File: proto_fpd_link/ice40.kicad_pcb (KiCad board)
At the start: 4 copper layers, 50 x 50 mm, 48 parts, among them J1 Conn_01x12, J101 Conn_02x05_Odd_Even, J102 Conn_01x18, J2 Conn_01x05, J3 Conn_01x19, J4 Conn_01x05, J5 Conn_01x01, J7 Conn_01x01, U101 TLV71333PDBV, U102 iCE40HX1K-CB132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

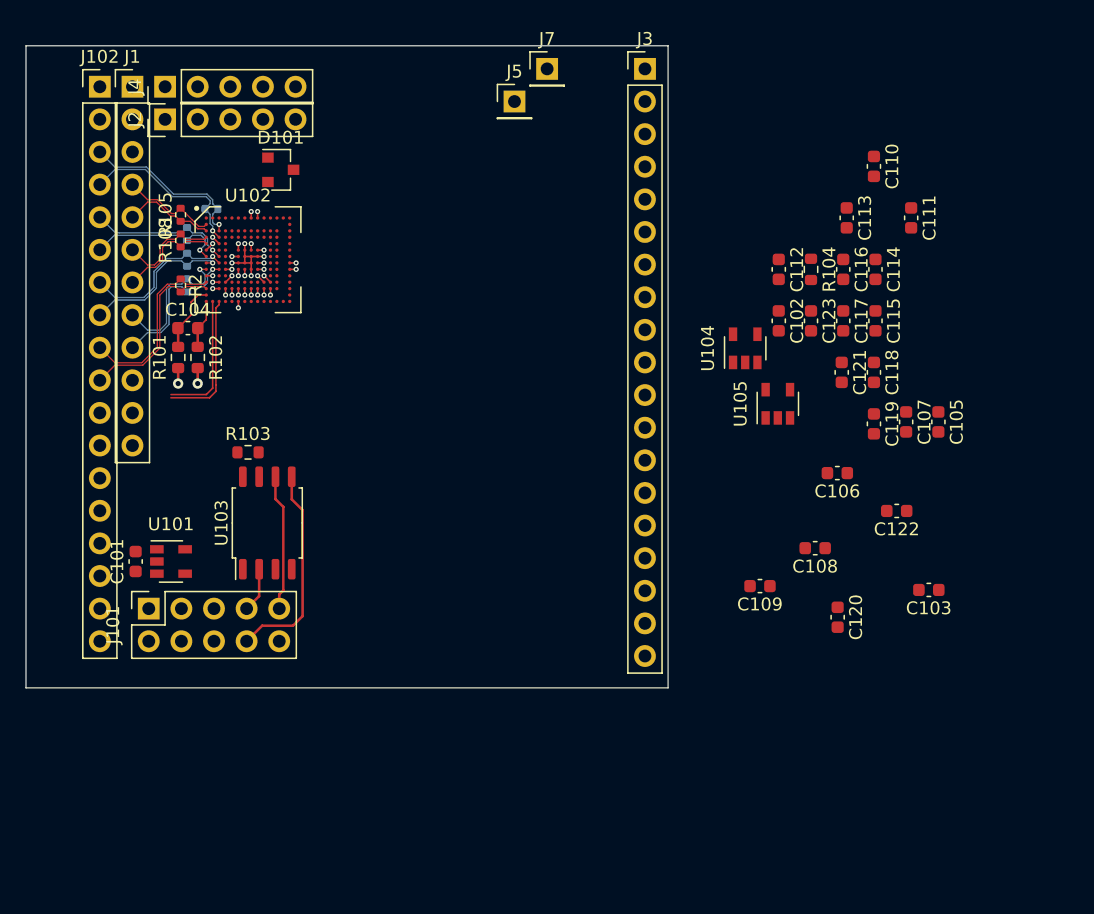
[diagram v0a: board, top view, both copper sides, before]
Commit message: initial commit of ice40 programmer board
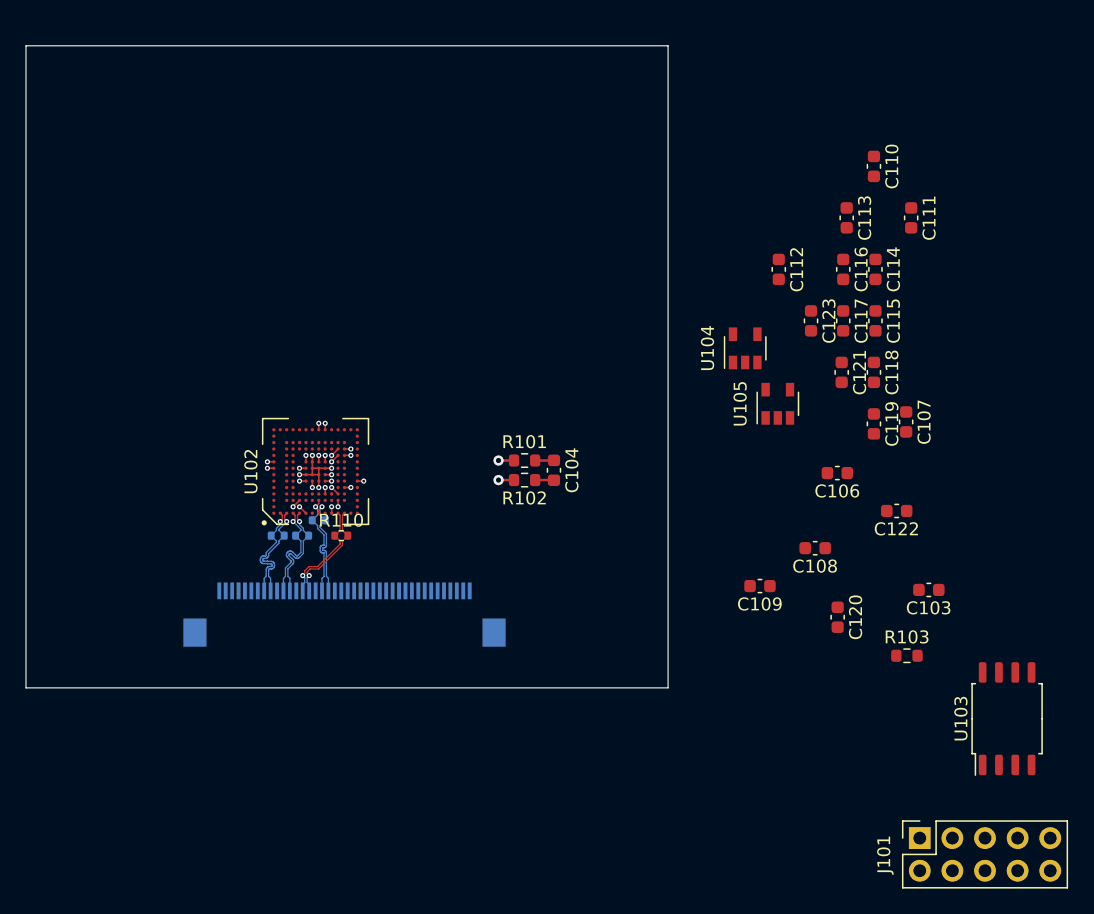
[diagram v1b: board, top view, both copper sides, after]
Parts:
- removed C101, C102, C105: 100n, Capacitor_SMD:C_0603_1608Metric
- removed D101: BAT54C, Package_TO_SOT_SMD:SOT-23
- removed J1: Conn_01x12, Connector_PinHeader_2.54mm:PinHeader_1x12_P2.54mm_Vertical
- removed J102: Conn_01x18, Connector_PinHeader_2.54mm:PinHeader_1x18_P2.54mm_Vertical
- removed J2, J4: Conn_01x05, Connector_PinHeader_2.54mm:PinHeader_1x05_P2.54mm_Vertical
- removed J3: Conn_01x19, Connector_PinHeader_2.54mm:PinHeader_1x19_P2.54mm_Vertical
- removed J5, J7: Conn_01x01, Connector_PinHeader_2.54mm:PinHeader_1x01_P2.54mm_Vertical
- removed R104: NM, Resistor_SMD:R_0603_1608Metric
- removed R111, R113, R2: 100R 1%, Resistor_SMD:R_0402_1005Metric
- removed U101: TLV71333PDBV, Package_TO_SOT_SMD:SOT-23-5
- added J6: Conn_01x40_MountingPin, Connector_FFC-FPC:Hirose_FH12-40S-0.5SH_1x40-1MP_P0.50mm_Horizontal, B.Cu at (148.1, 124.5)
- R105, R108: moved to B.Cu
- R110: moved to F.Cu
- moved J101 62.6 mm to (192.8, 141.9)
- moved U103 59.6 mm to (199.7, 132.7)
- moved R103 53.7 mm to (191.8, 127.8)
- moved C104 30.6 mm to (164.4, 113.3), turned to 270 degrees
- moved R101 28.1 mm to (162.1, 112.5), turned to 0 degrees
- moved R102 27.2 mm to (162.1, 114.1), turned to 180 degrees
- moved R106 26.4 mm to (144.8, 118.4)
- moved R105 26.1 mm to (142.8, 118.4), turned to 0 degrees
- moved R110 24.6 mm to (147.8, 118.4), turned to 0 degrees
- moved R108 24.3 mm to (146.1, 117.2), turned to 0 degrees
- moved U102 17.3 mm to (145.8, 113.4), turned to 90 degrees
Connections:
- R105 pad 1: /1- -> /Rxin0-
- R105 pad 2: /1+ -> /Rxin0+
- R106 pad 1: /2- -> /Rxin1-
- R106 pad 2: /2+ -> /Rxin1+
- R108 pad 1: /4- -> /RxCLK-
- R108 pad 2: /4+ -> /RxCLK+
- R110 pad 1: /6- -> /Rxin2-
- R110 pad 2: /6+ -> /Rxin2+
- U102 pad A14: Net-(D101-Pad3) -> +2V5
- U102 pad B1: /1+ -> /Rxin0-
- U102 pad C1: /1- -> /Rxin0+
- U102 pad C3: /2+ -> Net-(U102-PadC3)
- U102 pad D1: /4+ -> /Rxin1-
- U102 pad D3: /2- -> Net-(U102-PadD3)
- U102 pad E1: /4- -> /Rxin1+
- U102 pad G1: /7+ -> Net-(U102-PadG1)
- U102 pad G3: /7- -> Net-(U102-PadG3)
- U102 pad H1: /6- -> /RxCLK+
- U102 pad H3: /6+ -> /RxCLK-
- U102 pad J1: /9+ -> Net-(U102-PadJ1)
- U102 pad J3: /9- -> Net-(U102-PadJ3)
- U102 pad L1: /12- -> /Rxin2-
- U102 pad M1: /12+ -> /Rxin2+
- U104 pad 1: +3V3 -> +2V5
- U104 pad 3: +3V3 -> +2V5
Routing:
- net /SDO: track 16.9 -> 0.50 mm
- net /12+: track 14.1 -> 0.00 mm
- net /12-: track 14.1 -> 0.00 mm
- net /2-: track 13.6 -> 0.00 mm, vias 1 -> 0
- net /2+: track 13.5 -> 0.00 mm, vias 1 -> 0
- net /6+: track 12.4 -> 0.00 mm, vias 1 -> 0
- net /6-: track 12.2 -> 0.00 mm, vias 1 -> 0
- net /9-: track 11.6 -> 0.00 mm, vias 1 -> 0
- net /9+: track 11.3 -> 0.00 mm, vias 1 -> 0
- net /7-: track 11.2 -> 0.00 mm, vias 1 -> 0
- net /7+: track 10.9 -> 0.00 mm, vias 1 -> 0
- net /27: track 10.8 -> 0.00 mm
- net /SCK: track 10.7 -> 0.00 mm
- net /26: track 10.2 -> 0.00 mm
- net /Rxin0+: track 0.00 -> 8.55 mm, vias 0 -> 1
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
